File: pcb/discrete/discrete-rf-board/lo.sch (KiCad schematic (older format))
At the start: 37 parts

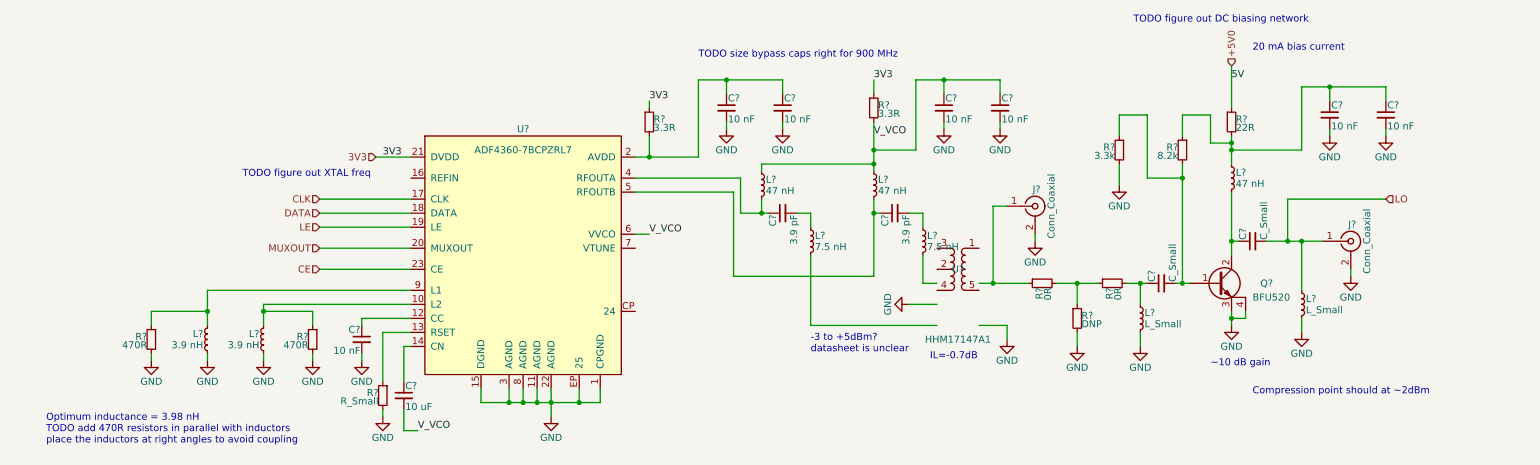
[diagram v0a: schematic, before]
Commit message: Finish first draft of LO amplifier
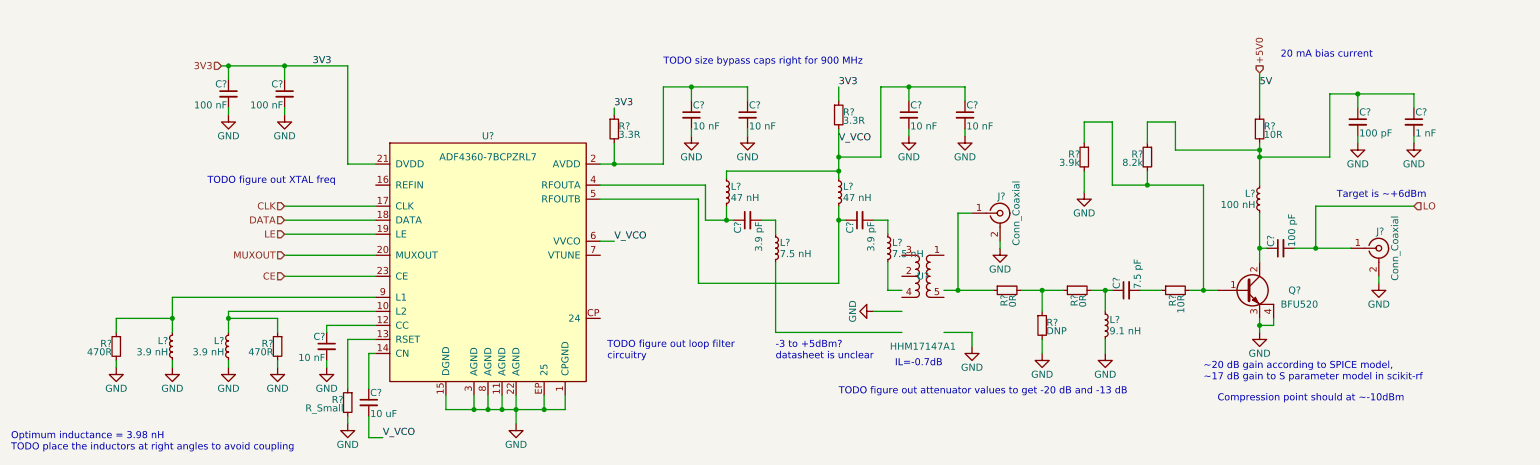
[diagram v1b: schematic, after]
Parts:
- removed L?: L_Small, symbol Device:L_Small
- added C? (x2): 100 nF, symbol Device:C_Small
- added R?: 10R, symbol Device:R_Small
- C?: value C_Small -> 7.5 pF
- C?: value C_Small -> 100 pF
- C?: value 10 nF -> 100 pF
- C?: value 10 nF -> 1 nF
- L?: value L_Small -> 9.1 nH
- L?: value 47 nH -> 100 nH
- R?: value 3.3k -> 3.9k
- R?: value 22R -> 10R
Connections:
- wire segments 145 -> 152
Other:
- note added: "Compression point should at ~~-10dBm"
- note added: "Optimum inductance = 3.98 nH\nTODO place the inductors at right angles to avoid coupling"
- note added: "TODO figure out attenuator values to get -20 dB and -13 dB"
- note added: "TODO figure out loop filter\ncircuitry"
- note added: "Target is ~~+6dBm"
- note added: "~~20 dB gain according to SPICE model,\n~~17 dB gain to S parameter model in scikit-rf"
- note removed: "Compression point should at ~~2dBm"
- note removed: "Optimum inductance = 3.98 nH\nTODO add 470R resistors in parallel with inductors\nplace the inductors at right angles to avoid coupling"
- note removed: "TODO figure out DC biasing network"
- note removed: "~~10 dB gain"
- moved on the sheet: C?, J?, L?, Q?, R?, U?

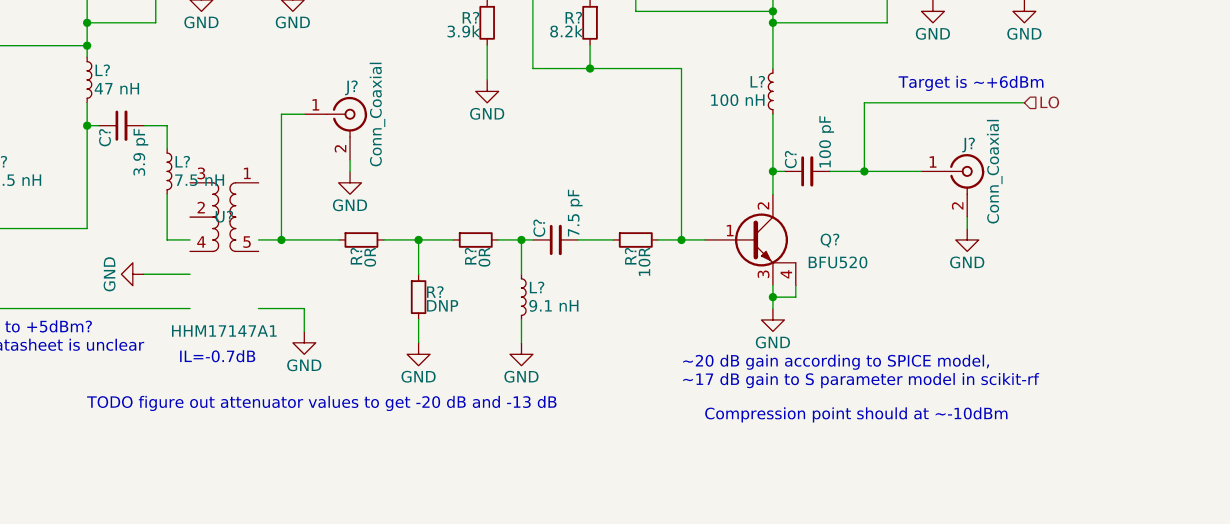
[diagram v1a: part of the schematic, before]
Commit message: Finish active mixer simulation; it looks good!
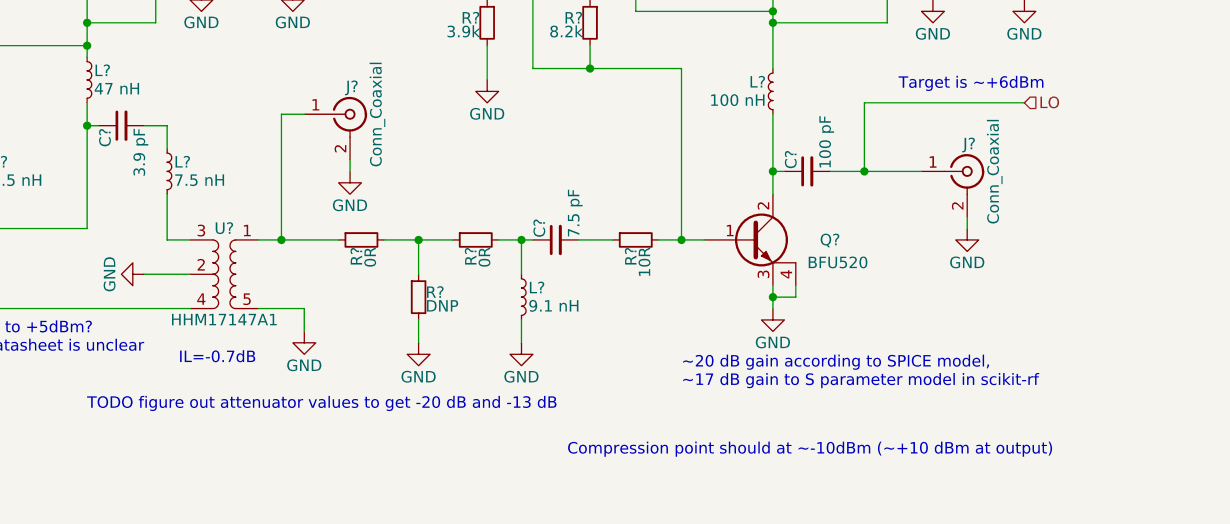
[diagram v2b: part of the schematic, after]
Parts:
- U?: Mouser (none) -> 810-HHM17147A1
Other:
- note added: "Compression point should at ~~-10dBm (~~+10 dBm at output)"
- note removed: "Compression point should at ~~-10dBm"
- moved on the sheet: U?
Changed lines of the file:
@@
 $Descr A4 11693 8268
 encoding utf-8
-Sheet 2 4
+Sheet 2 6
 Title ""
 Date ""
@@
 L discrete-parts:HHM17147A1 U?
 U 1 1 5CAFA1BF
-P 7050 4100
-F 0 "U?" H 7050 4100 50  0000 C CNN
-F 1 "HHM17147A1" H 7050 3600 50  0000 C CNN
-F 2 "" H 7050 4100 50  0001 C CNN
-F 3 "" H 7050 4100 50  0001 C CNN
-	1    7050 4100
+P 7050 4350
+AR Path="/5CAFA1BF" Ref="U?"  Part="1"
+AR Path="/5CA6B046/5CAFA1BF" Ref="U?"  Part="1"
+F 0 "U?" H 7050 4550 50  0000 C CNN
+F 1 "HHM17147A1" H 7050 4150 50  0000 C CNN
+F 2 "" H 7050 4350 50  0001 C CNN
+F 3 "" H 7050 4350 50  0001 C CNN
+F 4 "810-HHM17147A1" H 7050 4350 50  0001 C CNN "Mouser"
+	1    7050 4350
 	1    0    0    -1
 $EndComp
@@
 Text Notes 9600 2550 0    50   ~ 0
 20 mA bias current
-Text Notes 9150 5000 0    50   ~ 0
-Compression point should at ~~-10dBm
+Text Notes 8550 5150 0    50   ~ 0
+Compression point should at ~~-10dBm (~~+10 dBm at output)
 Text HLabel 9450 2650 1    50   Input ~ 0
 +5V0

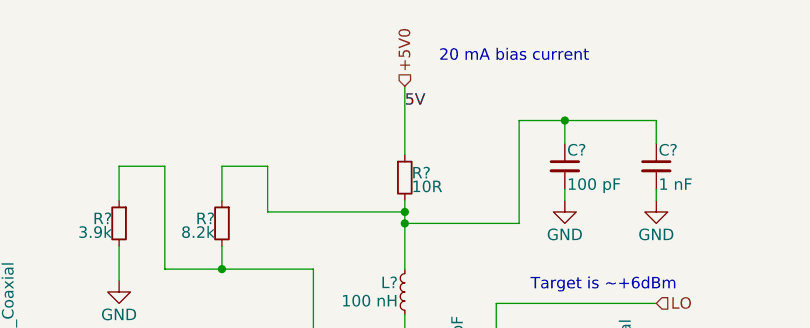
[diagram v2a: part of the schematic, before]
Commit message: Finish diode mixer simulations and capture in schematic
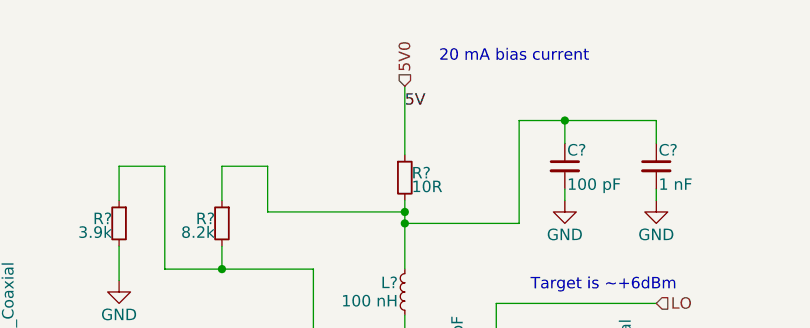
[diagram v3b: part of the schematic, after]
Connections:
- net +5V0 renamed 5V0
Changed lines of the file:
@@
 $Descr A4 11693 8268
 encoding utf-8
-Sheet 2 6
+Sheet 8 8
 Title ""
 Date ""
@@
 Compression point should at ~~-10dBm (~~+10 dBm at output)
 Text HLabel 9450 2650 1    50   Input ~ 0
-+5V0
+5V0
 Wire Wire Line
 	9450 2650 9450 2950

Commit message: Save changes while moving over to the new laptop
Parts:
- gave numbers to parts that had none: 39

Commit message: Merge stuff I guess, hopefully this doesn't break too much
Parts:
- renumbered C1001 to C1601, C1002 to C1602, C1003 to C1603, C1004 to C1604, C1005 to C1605, C1006 to C1606, C1007 to C1607, C1008 to C1608, C1009 to C1609, C1010 to C1610, C1011 to C1611, C1012 to C1612, C1013 to C1613, C1014 to C1614, J1001 to J1601, J1002 to J1602, L1001 to L1601, L1002 to L1602, L1003 to L1603, L1004 to L1604, L1005 to L1605, L1006 to L1606, L1007 to L1607, L1008 to L1608, Q1001 to Q1601, R1001 to R1601, R1002 to R1602, R1003 to R1603, R1004 to R1604, R1005 to R1605, R1006 to R1606, R1007 to R1607, R1008 to R1608, R1009 to R1609, R1010 to R1610, R1011 to R1611, R1012 to R1612, U1001 to U1601, U1002 to U1602
